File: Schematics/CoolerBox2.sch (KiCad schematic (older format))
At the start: 10 parts, among them J5 Conn_WallSocket_Earth, K2 JD2912-1Z-12VDC_40A, K3 JD2912-1Z-12VDC_40A, K4 FINDER-30.22, P2 Conn_WallPlug_Earth, U14 DPlusSimulator, U15 Inverter, U16 DometicCF35

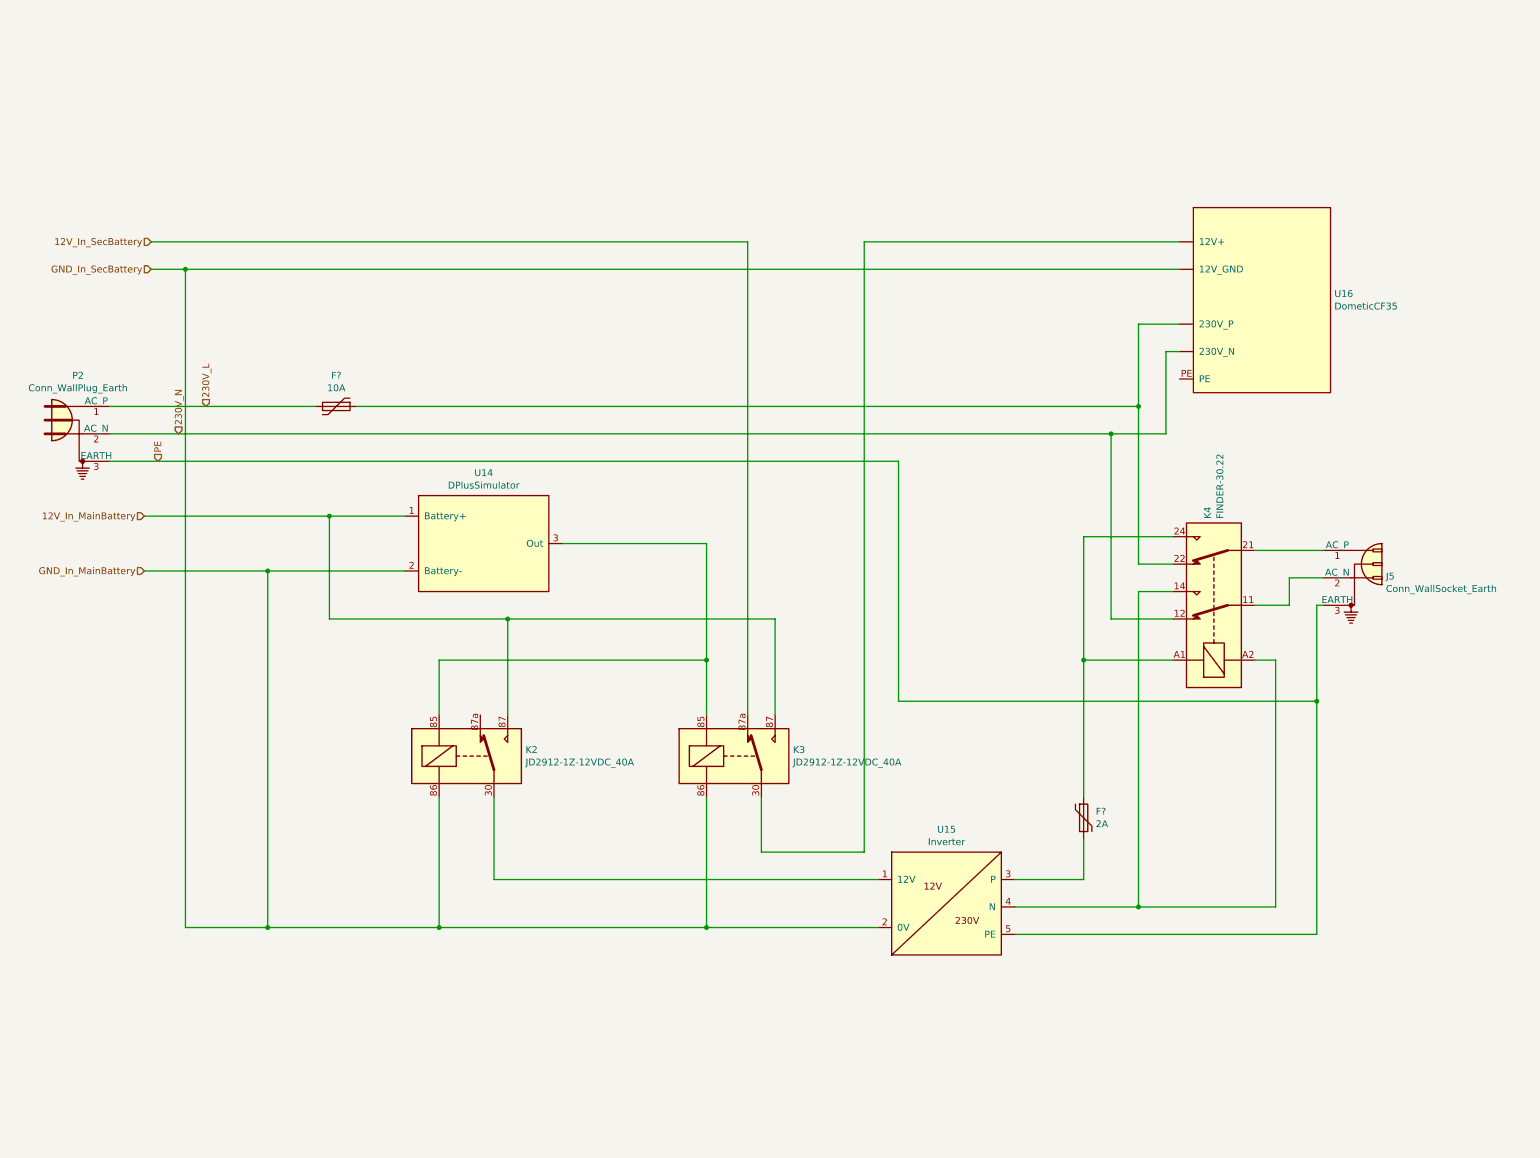
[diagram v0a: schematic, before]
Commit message: Add Kleinverteiler and snd. 230V conn
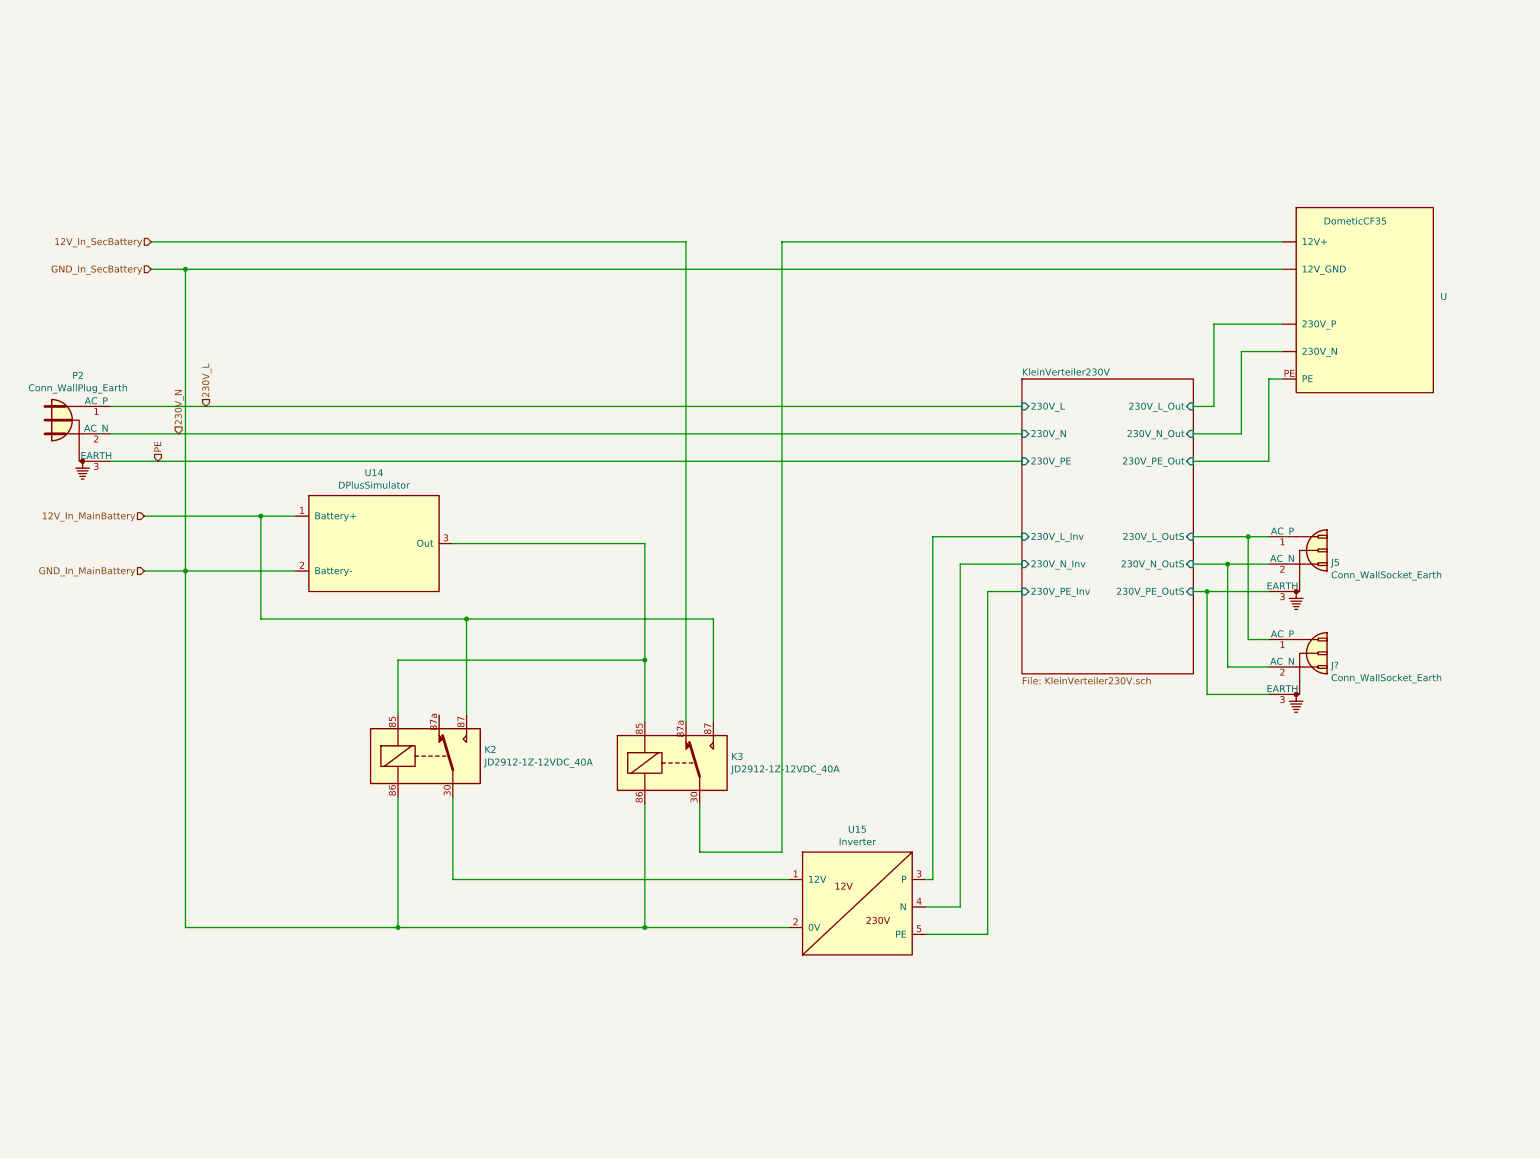
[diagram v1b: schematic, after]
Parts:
- removed F?: 10A, symbol Device:Polyfuse
- removed F?: 2A, symbol Device:Polyfuse
- removed K4: FINDER-30.22, Relay_THT:Relay_DPDT_Finder_30.22, symbol Relay:FINDER-30.22
- added J?: Conn_WallSocket_Earth, symbol Connector:Conn_WallSocket_Earth
- renumbered U16 to U
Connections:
- net 230V_N: no longer U.~ (230V_P)
- net PE: no longer J5.3 (EARTH), U15.5 (PE)
- net KleinVerteiler230V/230V_N_OutS: now reaches J5.2 (AC_N)
- net KleinVerteiler230V/230V_N_OutS: now also J?.2 (AC_N)
- net KleinVerteiler230V/230V_N_Inv: now reaches U15.4 (N)
- net KleinVerteiler230V/230V_L_OutS: now reaches J5.1 (AC_P)
- net KleinVerteiler230V/230V_L_OutS: now also J?.1 (AC_P)
- net KleinVerteiler230V/230V_N_Out: now reaches U.~ (230V_P)
- net KleinVerteiler230V/230V_PE_Out: now reaches U.PE
- net KleinVerteiler230V/230V_L_Inv: now reaches U15.3 (P)
- new net KleinVerteiler230V/230V_L_Out: U.~ (230V_P)
- new net KleinVerteiler230V/230V_PE_Inv: U15.5 (PE)
- new net KleinVerteiler230V/230V_PE_OutS: J5.3 (EARTH), J?.3 (EARTH)
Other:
- moved on the sheet: J5, K2, K3, U, U14, U15

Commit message: some modifications
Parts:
- gave numbers to parts that had none: 1
- renumbered J5 to J3, K2 to K1, K3 to K2, P2 to P1, U14 to U5, U15 to U6, U to U7
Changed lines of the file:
@@
 $Descr A4 11693 8268
 encoding utf-8
-Sheet 5 6
+Sheet 3 4
 Title ""
 Date ""
@@
 $EndDescr
 $Comp
-L MyParts:DPlusSimulator U14
+L MyParts:DPlusSimulator U5
 U 1 1 5F0EC705
 P 2650 3550
-F 0 "U14" H 3125 4415 50  0000 C CNN
+F 0 "U5" H 3125 4415 50  0000 C CNN
 F 1 "DPlusSimulator" H 3125 4324 50  0000 C CNN
 F 2 "" H 3800 4150 50  0001 C CNN
@@
 $EndComp
 $Comp
-L MyParts:JD2912-1Z-12VDC_40A K2
+L MyParts:JD2912-1Z-12VDC_40A K1
 U 1 1 5F0ECF0F
 P 3500 4750
-F 0 "K2" H 3930 4796 50  0000 L CNN
+F 0 "K1" H 3930 4796 50  0000 L CNN
 F 1 "JD2912-1Z-12VDC_40A" H 3930 4705 50  0000 L CNN
 F 2 "Relay_THT:Relay_StandexMeder_DIP_LowProfile" H 3950 4700 50  0001 L CNN
@@
 $EndComp
 $Comp
-L MyParts:JD2912-1Z-12VDC_40A K3
+L MyParts:JD2912-1Z-12VDC_40A K2
 U 1 1 5F0ED708
 P 5300 4800
-F 0 "K3" H 5730 4846 50  0000 L CNN
+F 0 "K2" H 5730 4846 50  0000 L CNN
 F 1 "JD2912-1Z-12VDC_40A" H 5730 4755 50  0000 L CNN
 F 2 "Relay_THT:Relay_StandexMeder_DIP_LowProfile" H 5750 4750 50  0001 L CNN
@@
 230V_N
 $Comp
-L Connector:Conn_WallSocket_Earth J5
+L Connector:Conn_WallSocket_Earth J3
 U 1 1 5F104118
 P 9850 3350
-F 0 "J5" H 10104 3361 50  0000 L CNN
+F 0 "J3" H 10104 3361 50  0000 L CNN
 F 1 "Conn_WallSocket_Earth" H 10104 3270 50  0000 L CNN
 F 2 "" H 9550 3450 50  0001 C CNN
@@
 PE
 $Comp
-L Connector:Conn_WallPlug_Earth P2
+L Connector:Conn_WallPlug_Earth P1
 U 1 1 5F0CAFB1
 P 900 2300
-F 0 "P2" H 967 2625 50  0000 C CNN
+F 0 "P1" H 967 2625 50  0000 C CNN
 F 1 "Conn_WallPlug_Earth" H 967 2534 50  0000 C CNN
 F 2 "" H 1300 2300 50  0001 C CNN
@@
 $EndComp
 $Comp
-L MyParts:Inverter U15
+L MyParts:Inverter U6
 U 1 1 5F1053BD
 P 6650 5500
-F 0 "U15" H 6650 5715 50  0000 C CNN
+F 0 "U6" H 6650 5715 50  0000 C CNN
 F 1 "Inverter" H 6650 5624 50  0000 C CNN
 F 2 "" H 6650 5500 50  0001 C CNN
@@
 	7600 3550 7600 6050
 $Comp
-L Connector:Conn_WallSocket_Earth J?
+L Connector:Conn_WallSocket_Earth J4
 U 1 1 5F1BD7BA
 P 9850 4100
-F 0 "J?" H 10104 4111 50  0000 L CNN
+F 0 "J4" H 10104 4111 50  0000 L CNN
 F 1 "Conn_WallSocket_Earth" H 10104 4020 50  0000 L CNN
 F 2 "" H 9550 4200 50  0001 C CNN
@@
 	9200 3550 9650 3550
 $Comp
-L MyParts:DometicCF35 U
+L MyParts:DometicCF35 U7
 U 1 1 5F0EFAA9
 P 10300 850
-F 0 "U" H 10900 300 50  0000 L CNN
+F 0 "U7" H 10900 300 50  0000 L CNN
 F 1 "DometicCF35" H 10050 850 50  0000 L CNN
 F 2 "" H 10300 850 50  0001 C CNN

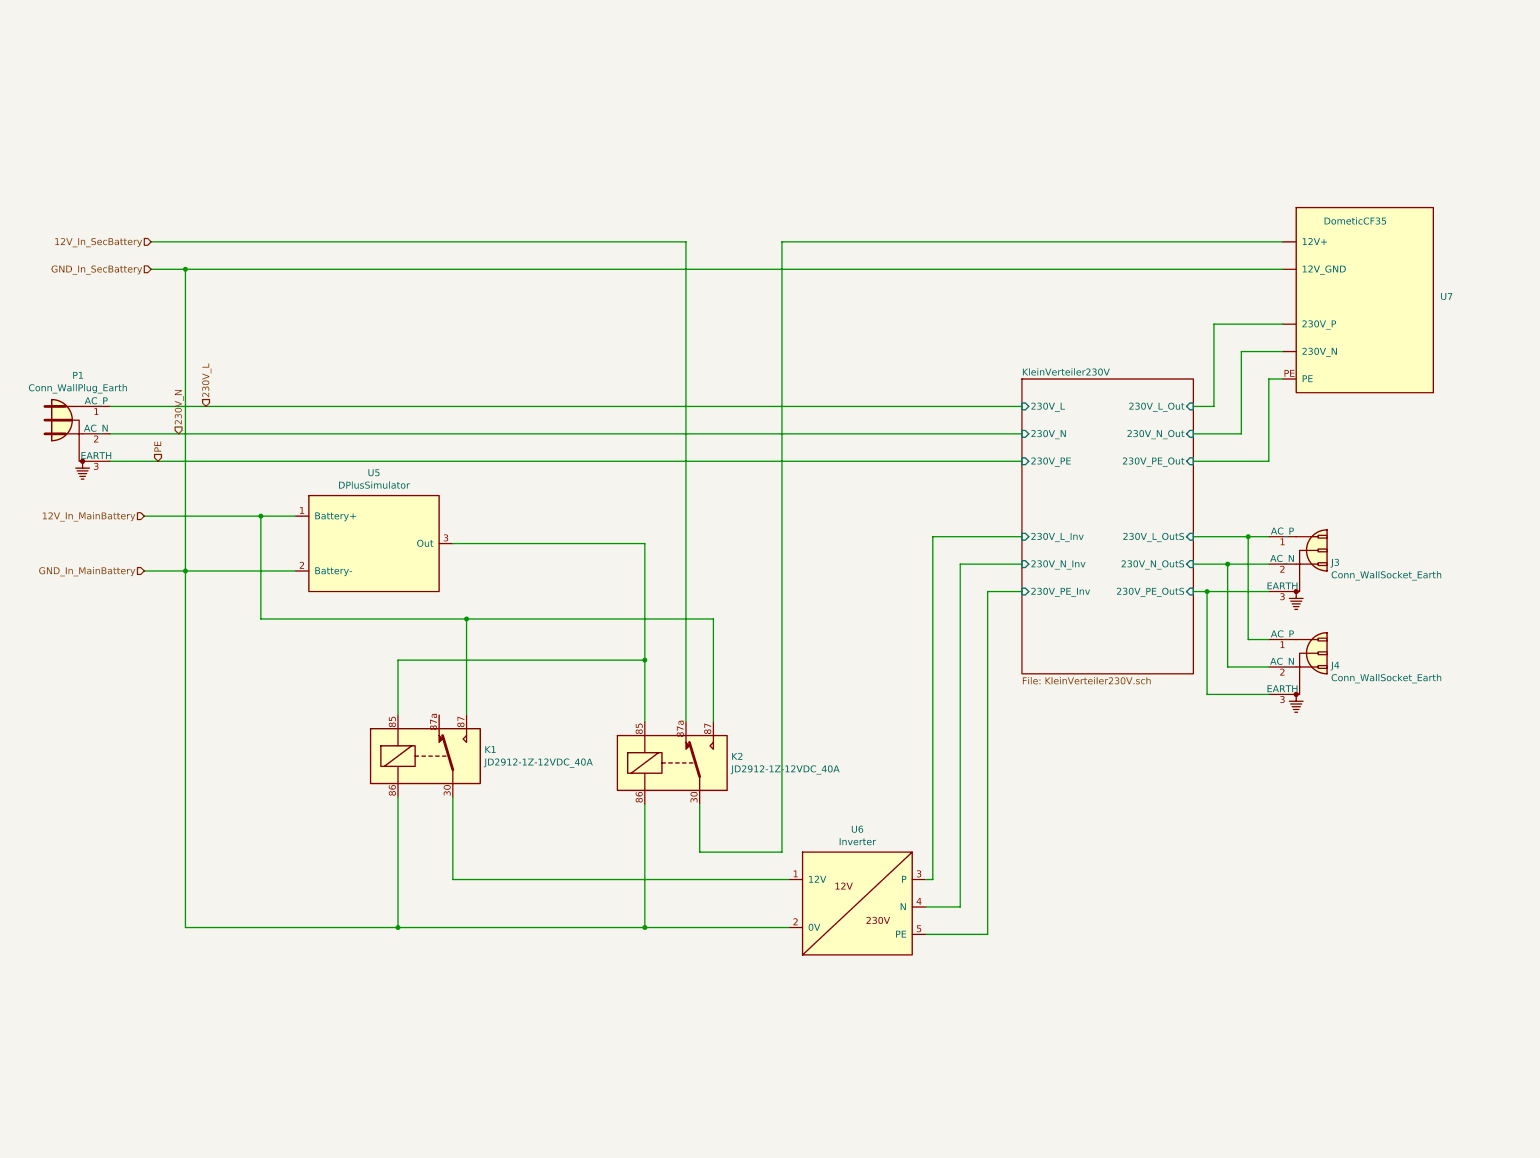
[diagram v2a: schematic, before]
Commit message: add terminal in Batterybox
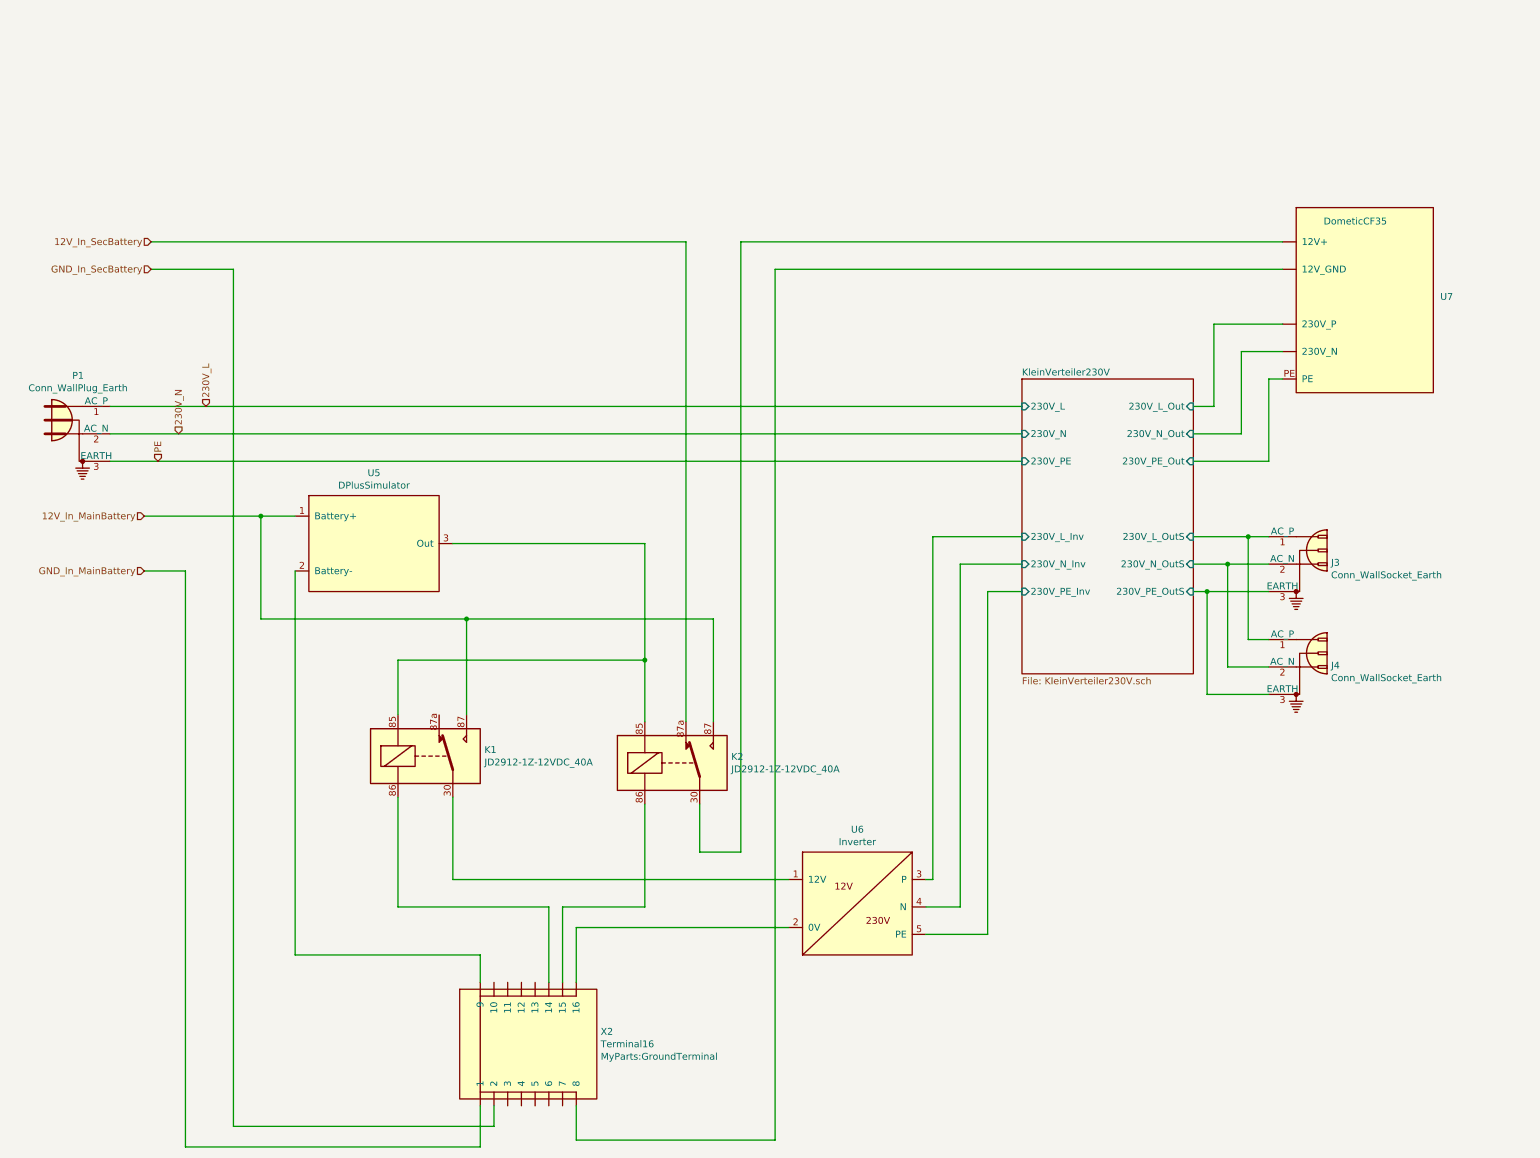
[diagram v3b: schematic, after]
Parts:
- added X2: Terminal16, MyParts:GroundTerminal, symbol MyParts:Terminal16
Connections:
- net GND_In_MainBattery: now also X2.~ (9); no longer K1.86, K2.86, U5.2 (Battery-), U6.2 (0V), U7.~ (230V_P)
- new net: U5.2 (Battery-), X2.~ (9)
- new net: K1.86, X2.~ (9)
- new net: K2.86, X2.~ (9)
- new net: U7.~ (230V_P), X2.~ (9)
- new net: U6.2 (0V), X2.~ (9)
- new net GND_In_SecBattery: X2.~ (9)
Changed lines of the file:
@@
 	5500 5100 5500 5450
 Wire Wire Line
-	5500 5450 6100 5450
-Wire Wire Line
-	6100 5450 6100 1000
-Wire Wire Line
-	6100 1000 9750 1000
+	5500 5450 5800 5450
+Wire Wire Line
+	5800 5450 5800 1000
+Wire Wire Line
+	5800 1000 9750 1000
 Text HLabel 1500 1000 0    50   Input ~ 0
 12V_In_SecBattery
@@
 Wire Wire Line
 	3700 5050 3700 5650
-Connection ~ 3300 6000
-Wire Wire Line
-	3300 5050 3300 6000
-Wire Wire Line
-	5100 5100 5100 6000
-Connection ~ 5100 6000
-Wire Wire Line
-	5100 6000 3300 6000
+Wire Wire Line
+	5100 5100 5100 5850
 Text HLabel 1900 2200 1    50   Input ~ 0
 230V_L
@@
 Wire Wire Line
 	7150 5650 7200 5650
-Wire Wire Line
-	5100 6000 6150 6000
-Wire Wire Line
-	1500 1200 1750 1200
-Wire Wire Line
-	1750 1200 1750 3400
-Connection ~ 1750 1200
-Wire Wire Line
-	1750 1200 9750 1200
 Wire Wire Line
 	7150 6050 7600 6050
@@
 	7600 3550 7850 3550
 Wire Wire Line
-	1750 6000 3300 6000
-Wire Wire Line
 	1450 3400 1750 3400
-Connection ~ 1750 3400
-Wire Wire Line
-	1750 3400 1750 6000
-Wire Wire Line
-	1750 3400 2550 3400
 Wire Wire Line
 	7200 3150 7200 5650
@@
 Wire Wire Line
 	9100 2600 9650 2600
+$Comp
+L MyParts:Terminal16 X2
+U 1 1 5F2891BD
+P 4350 6850
+F 0 "X2" H 4778 6941 50  0000 L CNN
+F 1 "Terminal16" H 4778 6850 50  0000 L CNN
+F 2 "MyParts:GroundTerminal" H 4778 6759 50  0000 L CNN
+F 3 "" H 4400 6900 50  0001 C CNN
+	1    4350 6850
+	1    0    0    -1
+$EndComp
+Wire Wire Line
+	1750 7600 3900 7600
+Wire Wire Line
+	3900 7600 3900 7300
+Wire Wire Line
+	3300 5850 4400 5850
+Wire Wire Line
+	1750 3400 1750 7600
+Wire Wire Line
+	3300 5050 3300 5850
+Wire Wire Line
+	5100 5850 4500 5850
+Wire Wire Line
+	6150 6000 4600 6000
+Wire Wire Line
+	1500 1200 2100 1200
+Wire Wire Line
+	2100 1200 2100 7450
+Wire Wire Line
+	2100 7450 4000 7450
+Wire Wire Line
+	4000 7450 4000 7300
+Wire Wire Line
+	2550 3400 2550 6200
+Wire Wire Line
+	2550 6200 3900 6200
+Wire Wire Line
+	4600 6000 4600 6400
+Wire Wire Line
+	4500 5850 4500 6400
+Wire Wire Line
+	4400 5850 4400 6400
+Wire Wire Line
+	3900 6200 3900 6400
+Wire Wire Line
+	4600 7300 4600 7550
+Wire Wire Line
+	4600 7550 6050 7550
+Wire Wire Line
+	6050 7550 6050 1200
+Wire Wire Line
+	6050 1200 9750 1200
 $EndSCHEMATC

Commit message: all in one Box
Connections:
- new net: U7.~ (230V_P), X2.~ (9)
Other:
- note added: "CoolerBox 1./2. Battery"
- note added: "Inverter"
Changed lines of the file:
@@
 Wire Wire Line
 	6050 1200 9750 1200
+Text Notes 2900 4450 0    50   ~ 0
+Inverter
+Text Notes 4650 4400 0    50   ~ 0
+CoolerBox 1./2. Battery
 $EndSCHEMATC

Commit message: Version 3
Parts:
- added K?: JD2912-1Z-12VDC_40A, Relay_THT:Relay_StandexMeder_DIP_LowProfile, symbol MyParts:JD2912-1Z-12VDC_40A
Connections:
- new net: U7.~ (230V_P), X2.~ (9)
- new net: K?.30, K?.31
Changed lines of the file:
@@
 $Descr A4 11693 8268
 encoding utf-8
-Sheet 3 4
+Sheet 3 5
 Title ""
 Date ""
@@
 Text Notes 4650 4400 0    50   ~ 0
 CoolerBox 1./2. Battery
+$Comp
+L MyParts:JD2912-1Z-12VDC_40A K?
+U 1 1 60AB0B75
+P 2650 -350
+F 0 "K?" H 3080 -304 50  0000 L CNN
+F 1 "JD2912-1Z-12VDC_40A" H 3080 -395 50  0000 L CNN
+F 2 "Relay_THT:Relay_StandexMeder_DIP_LowProfile" H 3100 -400 50  0001 L CNN
+F 3 "https://standexelectronics.com/wp-content/uploads/datasheet_reed_relay_DIP.pdf" H 2650 -350 50  0001 C CNN
+	1    2650 -350
+	1    0    0    -1
+$EndComp
 $EndSCHEMATC

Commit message: work on EoroBox
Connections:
- new net: U7.~ (230V_P), X2.~ (9)
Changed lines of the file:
@@
 $Descr A4 11693 8268
 encoding utf-8
-Sheet 3 5
+Sheet 3 9
 Title ""
 Date ""
